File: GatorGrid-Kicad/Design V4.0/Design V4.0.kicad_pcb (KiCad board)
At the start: 2 copper layers, 92 x 114 mm, 35 parts, among them J1 Battery-Connector, J2 Conn_01x20_Pin, J3 Conn_01x20_Pin, J4 Conn_01x20_Pin, J5 Conn_01x20_Pin, J7 Conn_01x03, Q3 2N3904, Q4 2N3904, SW1 SW_SPST, U1 TP4056

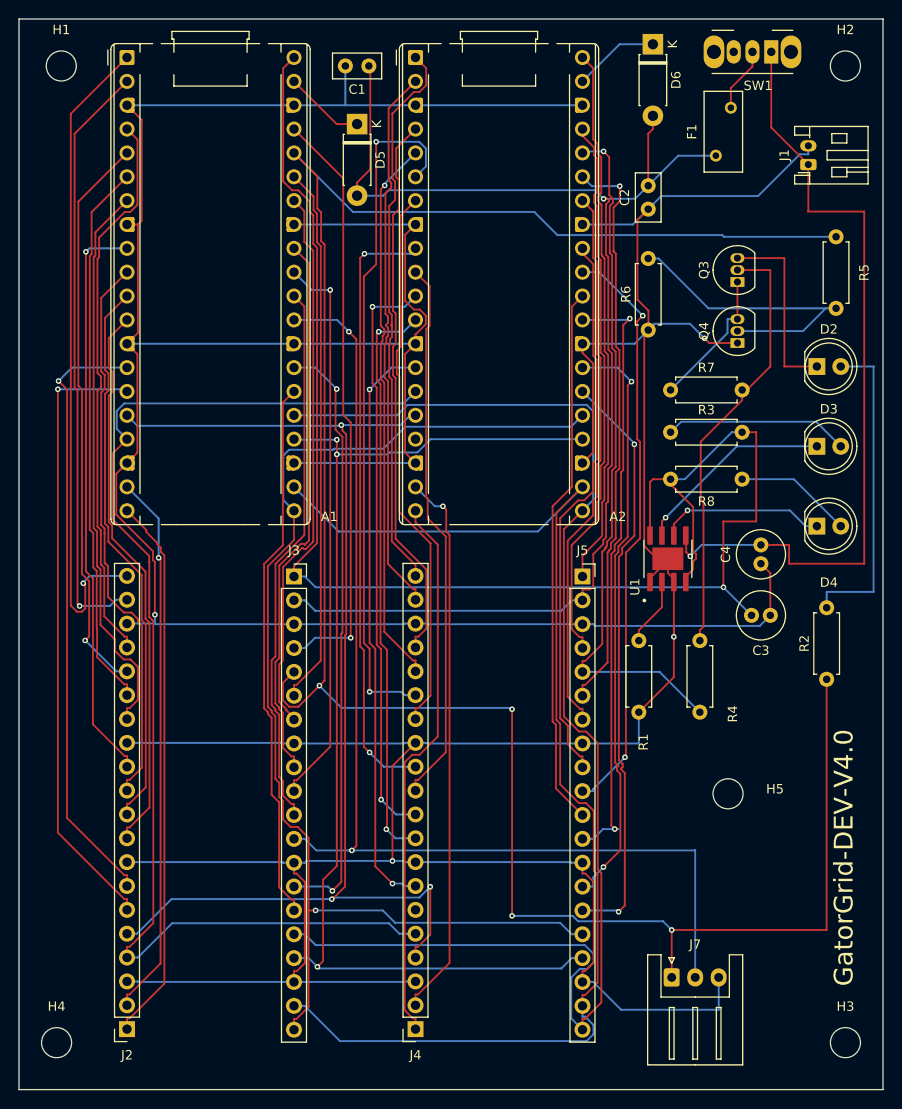
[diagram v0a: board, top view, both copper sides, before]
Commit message: Moved around some components in the PCB
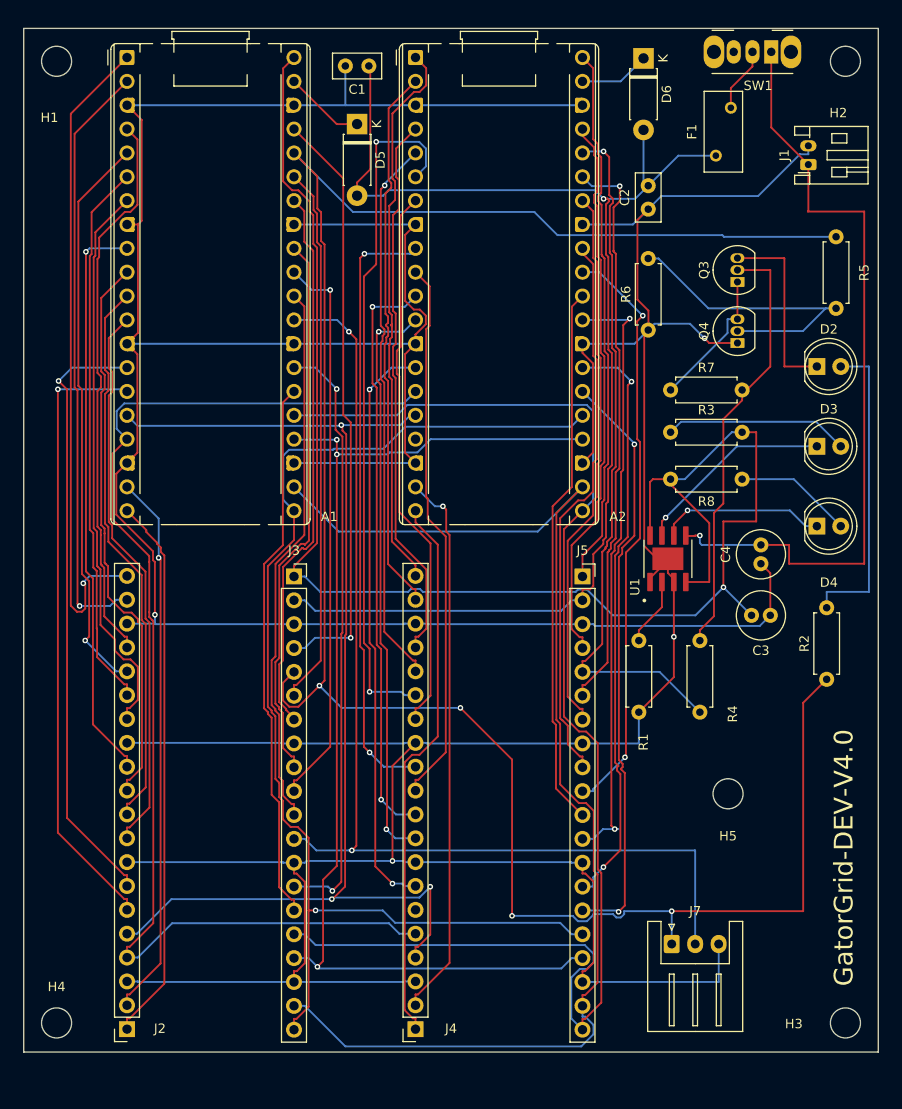
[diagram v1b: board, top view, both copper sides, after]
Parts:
- moved J7 3.56 mm to (227.0, 127.0)
- moved H3 2.10 mm to (245.5, 135.4)
- moved H4 2.10 mm to (161.5, 135.4)
- moved D6 1.80 mm to (224.0, 32.7)
- moved H1 0.71 mm to (161.5, 33.0)
- moved H2 0.50 mm to (245.5, 33.0)
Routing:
- net A_3V3(OUT): track 237.8 -> 230.2 mm
- net A-VBUS: track 160.8 -> 166.4 mm
- net SENSOR_DATA: track 119.9 -> 115.6 mm
- net Net-(A2-VSYS): track 9.14 -> 7.51 mm
- net VBAT(+): track 85.6 -> 84.1 mm
- net VSYS: track 139.9 -> 138.4 mm
- net Net-(D2-A): track 34.2 -> 33.2 mm
- net GND: track 593.9 -> 593.2 mm
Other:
- board size 92 x 114 mm -> 91 x 109 mm

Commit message: Finihsed design
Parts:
- moved R1 1.50 mm to (225.0, 102.3)
- moved U1 0.58 mm to (226.5, 85.4), turned to 0 degrees
- moved H3 0.40 mm to (245.5, 135.0)
- moved H4 0.40 mm to (161.5, 135.0)
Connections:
- A1 pad 16: UART_TX -> A_GPIO12
- A1 pad 17: UART_RX -> A_GPIO13
- A1 pad 21: RX-TX -> A_GPIO16
- A1 pad 22: CS -> A_GPIO17
- A1 pad 24: SCK -> A_GPIO18
- A1 pad 25: TX-RX -> A_GPIO19
- A1 pad 6: A_GPIO4 -> UART_TX
- A1 pad 7: A_GPIO5 -> UART_RX
- A2 pad 15: UART_RX -> B_GPIO11
- A2 pad 16: UART_TX -> B_GPIO12
- A2 pad 21: TX-RX -> B_GPIO16
- A2 pad 22: CS -> B_GPIO17
- A2 pad 24: SCK -> B_GPIO18
- A2 pad 25: RX-TX -> B_GPIO19
- A2 pad 6: B_GPIO4 -> UART_RX
- A2 pad 7: B_GPIO5 -> UART_TX
- J2 pad 1: A_GPIO15 -> A_GPIO0
- J2 pad 10: A_GPIO8 -> A_GPIO7
- J2 pad 11: A_GPIO7 -> A_GPIO8
- J2 pad 12: A_GPIO6 -> A_GPIO9
- J2 pad 14: A_GPIO5 -> A_GPIO10
- J2 pad 15: A_GPIO4 -> A_GPIO11
- J2 pad 16: A_GPIO3 -> A_GPIO12
- J2 pad 17: A_GPIO2 -> A_GPIO13
- J2 pad 19: A_GPIO1 -> A_GPIO14
- J2 pad 2: A_GPIO14 -> A_GPIO1
- J2 pad 20: A_GPIO0 -> A_GPIO15
- J2 pad 4: UART_RX -> A_GPIO2
- J2 pad 5: UART_TX -> A_GPIO3
- J2 pad 6: A_GPIO11 -> UART_TX
- J2 pad 7: A_GPIO10 -> UART_RX
- J2 pad 9: A_GPIO9 -> A_GPIO6
- J3 pad 1: A-VBUS -> A_GPIO16
- J3 pad 10: A_GPIO26 -> A_RUN
- J3 pad 11: A_RUN -> A_GPIO26
- J3 pad 12: SENSOR_DATA -> A_GPIO27
- J3 pad 14: A_GPIO21 -> A_GPIO28
- J3 pad 15: A_GPIO20 -> A_ADC_VREF
- J3 pad 16: TX-RX -> A_3V3(OUT)
- J3 pad 17: SCK -> A_3V3_EN
- J3 pad 19: CS -> VSYS
- J3 pad 2: VSYS -> A_GPIO17
- J3 pad 20: RX-TX -> A-VBUS
- J3 pad 4: A_3V3_EN -> A_GPIO18
- J3 pad 5: A_3V3(OUT) -> A_GPIO19
- J3 pad 6: A_ADC_VREF -> A_GPIO20
- J3 pad 7: A_GPIO28 -> A_GPIO21
- J3 pad 9: A_GPIO27 -> SENSOR_DATA
- J4 pad 1: B_GPIO15 -> B_GPIO0
- J4 pad 10: B_GPIO8 -> B_GPIO7
- J4 pad 11: B_GPIO7 -> B_GPIO8
- J4 pad 12: B_GPIO6 -> B_GPIO9
- J4 pad 14: B_GPIO5 -> B_GPIO10
- J4 pad 15: B_GPIO4 -> B_GPIO11
- J4 pad 16: B_GPIO3 -> B_GPIO12
- J4 pad 17: B_GPIO2 -> B_GPIO13
- J4 pad 19: B_GPIO1 -> B_GPIO14
- J4 pad 2: B_GPIO14 -> B_GPIO1
- J4 pad 20: B_GPIO0 -> B_GPIO15
- J4 pad 4: UART_TX -> B_GPIO2
- J4 pad 5: UART_RX -> B_GPIO3
- J4 pad 6: B_GPIO11 -> UART_RX
- J4 pad 7: B_GPIO10 -> UART_TX
- J4 pad 9: B_GPIO9 -> B_GPIO6
- J5 pad 1: B-VBUS -> B_GPIO16
- J5 pad 10: B_GPIO26 -> B_RUN
- J5 pad 11: B_RUN -> B_GPIO26
- J5 pad 12: B_GPIO22 -> B_GPIO27
- J5 pad 14: B_GPIO21 -> B_GPIO28
- J5 pad 15: B_GPIO20 -> B_ADC_VREF
- J5 pad 16: RX-TX -> B_3V3(OUT)
- J5 pad 17: SCK -> B_3V3_EN
- J5 pad 19: CS -> VSYS
- J5 pad 2: VSYS -> B_GPIO17
- J5 pad 20: TX-RX -> B-VBUS
- J5 pad 4: B_3V3_EN -> B_GPIO18
- J5 pad 5: B_3V3(OUT) -> B_GPIO19
- J5 pad 6: B_ADC_VREF -> B_GPIO20
- J5 pad 7: B_GPIO28 -> B_GPIO21
- J5 pad 9: B_GPIO27 -> B_GPIO22
- J7 pad 1: A_3V3(OUT) -> SENSOR_DATA
- J7 pad 2: SENSOR_DATA -> A_3V3(OUT)
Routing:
- net TX-RX: track 145.6 -> 0.00 mm
- net CS: track 132.1 -> 0.00 mm
- net RX-TX: track 129.7 -> 0.00 mm, vias 1 -> 0
- net SCK: track 120.0 -> 0.00 mm, vias 3 -> 0
- net B_GPIO4: track 73.5 -> 0.00 mm, vias 2 -> 0
- net A_GPIO5: track 59.7 -> 0.00 mm
- net A_GPIO4: track 58.7 -> 0.00 mm
- net B_GPIO5: track 58.4 -> 0.00 mm
- net A-VBUS: track 166.4 -> 219.3 mm, vias 1 -> 3
- net B_GPIO15: track 58.7 -> 6.94 mm
- net B-VBUS: track 57.8 -> 109.6 mm
- net A_GPIO15: track 58.7 -> 6.94 mm
- net B_GPIO0: track 59.3 -> 108.1 mm
- net B_GPIO14: track 58.9 -> 13.2 mm, vias 1 -> 0
- net A_GPIO14: track 58.3 -> 13.2 mm, vias 1 -> 0
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
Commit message: Finished Kicad
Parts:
- R3, R8: value 1k -> 220
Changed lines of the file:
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@@
 			)
 		)
-		(property "Value" "1k"
+		(property "Value" "220"
 			(at 10.81 5 0)
 			(layer "F.Fab")
@@
 			)
 		)
-		(property "Value" "1k"
+		(property "Value" "220"
 			(at 10.31 5 0)
 			(layer "F.Fab")
